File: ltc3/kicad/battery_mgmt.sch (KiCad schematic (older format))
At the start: 81 parts, among them Q1 Q_NMOS_DGS, Q2 Q_NMOS_DGS, Q3 Q_NMOS_DGS, Q4 Q_NMOS_DGS

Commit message: Deleted "Power Sources" sheet.
Moved what little circuity it contained into the "Battery Charging"
and "Battery Balancing" sheets.
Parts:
- added P?: LAB_IN, symbol CONN_01X02
- added R? (x2): R4T, symbol R4T
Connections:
- net labels added: BB_VSENSE_BATT+, BB_VSENSE_BATT-, BB_VSENSE_PV+, BB_VSENSE_PV-, VCC_BATT
- wire segments 204 -> 218
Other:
- note added: "R_sense = 1/Imax**2\n1 A = 1 ohm\n3 A = 0.1 ohm\n5 A = 0.04 ohms\n10 A = 0.01 ohms"
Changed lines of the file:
@@
 $Descr B 17000 11000
 encoding utf-8
-Sheet 8 9
-Title "Battery Charging"
+Sheet 8 8
+Title "Power In, Battery Management"
 Date "2015-10-24"
 Rev "A"
@@
 	1    0    0    -1
 $EndComp
-Text Notes 1400 9500 0    100  ~ 0
+Text Notes 2900 10250 0    100  ~ 0
 TODO:\n* Add feedback resistor disconnect circuit (datasheet fig. 27).
 Text Label 15350 8200 0    60   ~ 0
@@
 Text Label 5850 2550 2    60   ~ 0
 CSP
+$Comp
+L CONN_01X02 P?
+U 1 1 56357D56
+P 850 9850
+F 0 "P?" H 850 10000 50  0000 C CNN
+F 1 "LAB_IN" V 950 9850 50  0000 C CNN
+F 2 "" H 850 9850 60  0000 C CNN
+F 3 "" H 850 9850 60  0000 C CNN
+	1    850  9850
+	-1   0    0    1
+$EndComp
+Connection ~ 2050 9000
+Wire Wire Line
+	2050 9000 2050 9550
+Wire Wire Line
+	1950 9000 2300 9000
+Wire Wire Line
+	1300 9000 1650 9000
+Text HLabel 2300 9300 2    60   Output ~ 0
+BB_VSENSE_PV-
+Text HLabel 2300 9200 2    60   Output ~ 0
+BB_VSENSE_PV+
+$Comp
+L R4T R?
+U 1 1 5635AA23
+P 1800 9000
+F 0 "R?" V 1750 8850 50  0000 C CNN
+F 1 "R4T" V 1800 9000 50  0000 C CNN
+F 2 "" V 1730 9000 30  0000 C CNN
+F 3 "" H 1800 9000 30  0000 C CNN
+F 4 "1W 1%" V 1700 9100 60  0000 C CNN "Note"
+	1    1800 9000
+	0    1    1    0
+$EndComp
+Wire Wire Line
+	2300 9200 1750 9200
+Wire Wire Line
+	1750 9200 1750 9100
+Wire Wire Line
+	1850 9100 1850 9300
+Wire Wire Line
+	1850 9300 2300 9300
+Text HLabel 15400 700  2    60   Output ~ 0
+VCC_BATT
+Connection ~ 15150 700
+Wire Wire Line
+	15150 700  15150 1250
+Wire Wire Line
+	15050 700  15400 700
+Wire Wire Line
+	14400 700  14750 700
+Text HLabel 15400 1000 2    60   Output ~ 0
+BB_VSENSE_BATT-
+Text HLabel 15400 900  2    60   Output ~ 0
+BB_VSENSE_BATT+
+Text Notes 14750 2250 0    100  ~ 0
+R_sense = 1/Imax**2\n1 A = 1 ohm\n3 A = 0.1 ohm\n5 A = 0.04 ohms\n10 A = 0.01 ohms
+$Comp
+L R4T R?
+U 1 1 5635B0F2
+P 14900 700
+F 0 "R?" V 14850 550 50  0000 C CNN
+F 1 "R4T" V 14900 700 50  0000 C CNN
+F 2 "" V 14830 700 30  0000 C CNN
+F 3 "" H 14900 700 30  0000 C CNN
+F 4 "1W 1%" V 14800 800 60  0000 C CNN "Note"
+	1    14900 700
+	0    1    1    0
+$EndComp
+Wire Wire Line
+	15400 900  14850 900
+Wire Wire Line
+	14850 900  14850 800
+Wire Wire Line
+	15400 1000 14950 1000
+Wire Wire Line
+	14950 1000 14950 800
 $EndSCHEMATC

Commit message: More progress on cleaning up battery management circuit.
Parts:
- removed C?: 470n, symbol C
- removed Ccspout?, Cout?: C, symbol C
- removed R?: 10, symbol R
- removed Rsense?: 4.36m, symbol R
- added COUT4: 1μ, symbol C
- renumbered Cout1 to COUT1, Cout2a to COUT2A, Cout2b to COUT2B
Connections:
- net labels added: EXTVCC
- wire segments 218 -> 293
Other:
- moved on the sheet: C?, CCSPOUT, COUT1, COUT2A, COUT2B, R?, Rsense?

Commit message: Finished cleaning up battery management (LT8490) schematic.
High probability of errors, and certainly still room for improvement,
but I want to get the work on this branch merged back to the trunk.
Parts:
- removed Rsense?: 21m, symbol R
- removed Rsense?: 4.36m, symbol R
- added C?: 68n, symbol C
- added CIN4: 2.2µ, symbol C
- added R?: 53.6k, symbol R
- R?: value R4T -> 21m
- R?: value R4T -> 4.36m
- gave numbers to parts that had none: 1
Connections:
- net labels added: /SHDN, EXTV_CC, FAULT, FBIN, FBIW, RT, STATUS, VIN, VINR, VOUT
- net labels removed: Battery(+), PV+
- wire segments 293 -> 212
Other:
- note added: "FIXME: Safe to use one current-sense resistor\n for both the LT8490 and the LTC2991?"
- note added: "Place close to VIN."
- note removed: "R_sense = 1/Imax**2\n1 A = 1 ohm\n3 A = 0.1 ohm\n5 A = 0.04 ohms\n10 A = 0.01 ohms"
- moved on the sheet: C?, CCSPOUT, CIN1A, CIN1B, CIN1C, CIN2A, CIN2B, CIN2C, CIN3A, CIN3B, COUT1, COUT2A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

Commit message: More clean-up of battery-related sheets.
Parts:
- gave numbers to parts that had none: 6
- renumbered CIN1C to C?, CIN2C to C?, CIN3A to C?, COUT3B to C?, COUT2A to C?, COUT1 to C?, COUT2B to C?, CIN1B to C?, CIN1A to C?, CIN2B to C?, CIN2A to C?, CIN3B to C?, CCSPOUT to C?, COUT3A to C?, CIN4 to C?, COUT4 to C?, DB1 to D?, DB2 to D?
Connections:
- net BB_VSENSE_BATT+ renamed CSPOUT
- net BB_VSENSE_BATT- renamed CSNOUT
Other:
- note added: "CCSPOUT"
- note added: "CIN1"
- note added: "CIN2"
- note added: "CIN3"
- note added: "CIN4"
- note added: "COUT1"
- note added: "COUT2"
- note added: "COUT3"
- note added: "Place close\nto VIN."
- note removed: "Place close to VIN."
- moved on the sheet: C?, P?

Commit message: Re-ordered LTC3 schematic sheets; annotated battery management components.
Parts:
- gave numbers to parts that had none: 76
- renumbered L1 to L201, Q1 to Q201, Q4 to Q202, Q2 to Q203, Q3 to Q204

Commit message: LTC3: Updated batt mgmt feedback component values.
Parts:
- C223: renamed from C225; value .2532 µF -> .18µ
- C231: renamed from C226; value .3013µF -> .33µ
- R208: renamed from R224; Note (none) -> 1%
- R210: renamed from R228; value 8.06k -> 8k06; Note (none) -> 1%
- R214: renamed from R213; value 203.92k -> 294k
- R216: value 7.899k -> 11k5
- R217: value 39.49k -> 57k6
- R220: renamed from R219; value 7k -> 10k2
- R221: renamed from Rfbin201; value 94.725k -> 93k1
- R223: renamed from R214; value 7.731k -> 7k68
- R224: renamed from R215; value 16.592k -> 16k5
- R227: renamed from R218; value 3.318k -> 3k32
- renumbered C223 to C220, C224 to C221, C227 to C224, C228 to C225, C229 to C226, C230 to C227, C231 to C228, C220 to C229, C221 to C230, D203 to D201, D204 to D202, D201 to D203, D202 to D204, R208 to R209, R209 to R213, R225 to R215, R210 to R218, R229 to R219, R220 to R222, R222 to R225, R223 to R226, R226 to R228, R227 to R229, R221 to R233, R233 to R234
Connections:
- net GND: now also R223.2; no longer C231.2
- net /SHDN: no longer names the net of R215.2, R219.1, U201.11 (SHDN)
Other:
- note added: "202kHz switch"
- note added: "CDACI"
- note added: "RDAC01"
- note added: "RDAC02"
- note added: "RDACI1"
- note added: "RDACI2"
- note added: "RFBIN1"
- note added: "RFBIN2"
- note added: "RFBOUT1"
- note added: "RFBOUT2"
- note added: "TODO:\n* Add DC supply detection circuit (datasheet p. 35).\n* Add feedback resistor disconnect circuit (datasheet fig. 27)."
- note removed: "TODO:\n* Add feedback resistor disconnect circuit (datasheet fig. 27)."
- moved on the sheet: C201, C202, C203, C204, C205, C206, C207, C208, C209, C210, C211, C212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

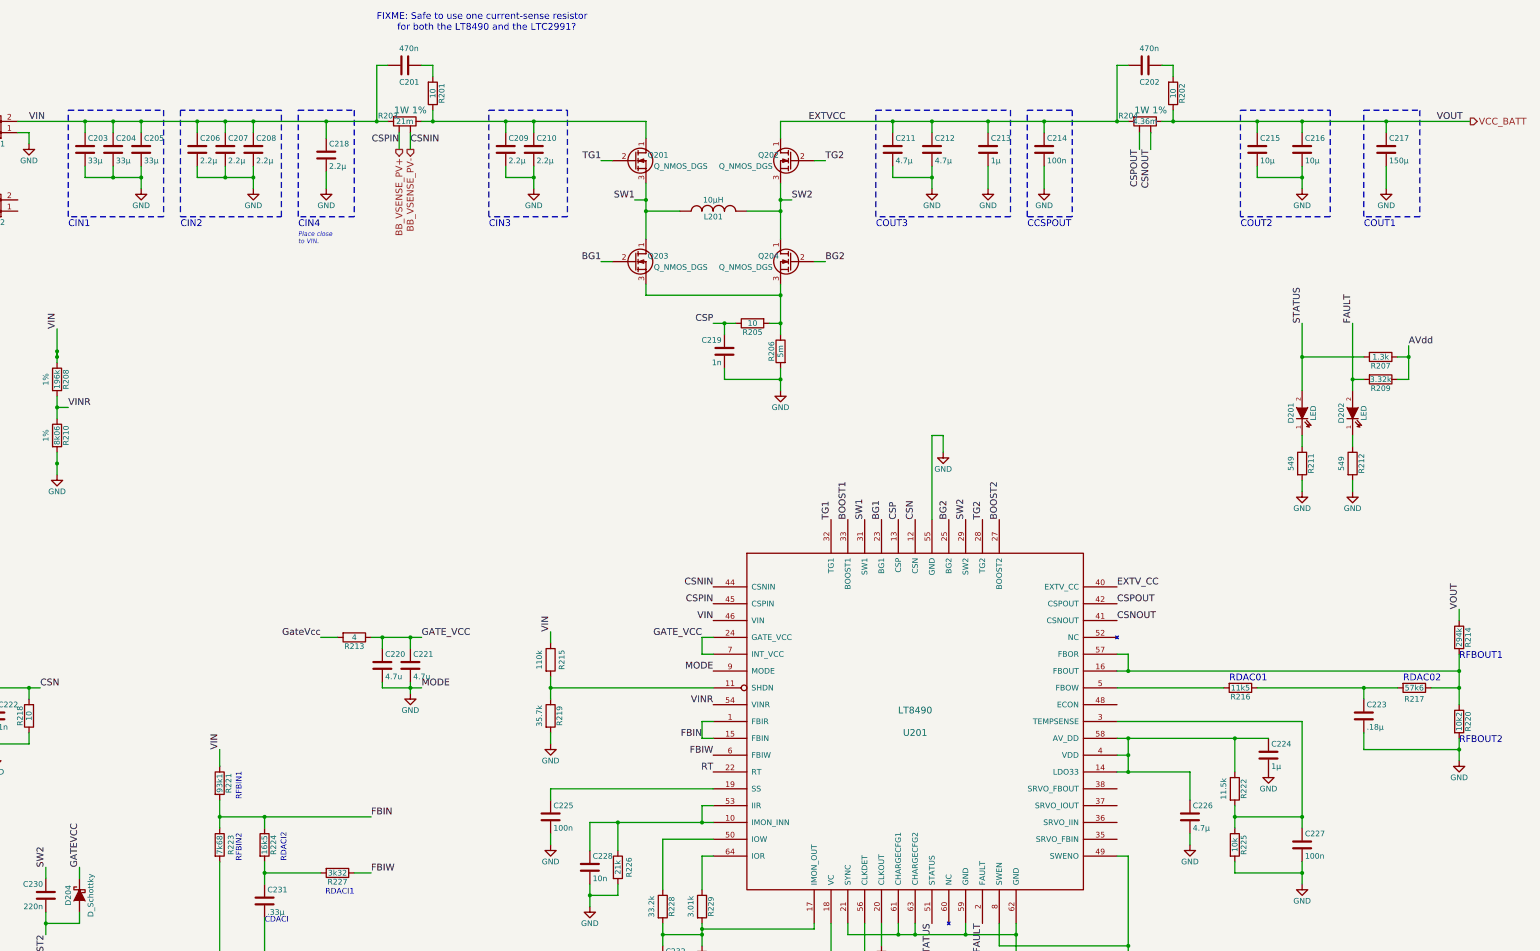
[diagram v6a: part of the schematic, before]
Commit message: LTC3: First take at adding datasheet references to batt mgmt schematic.
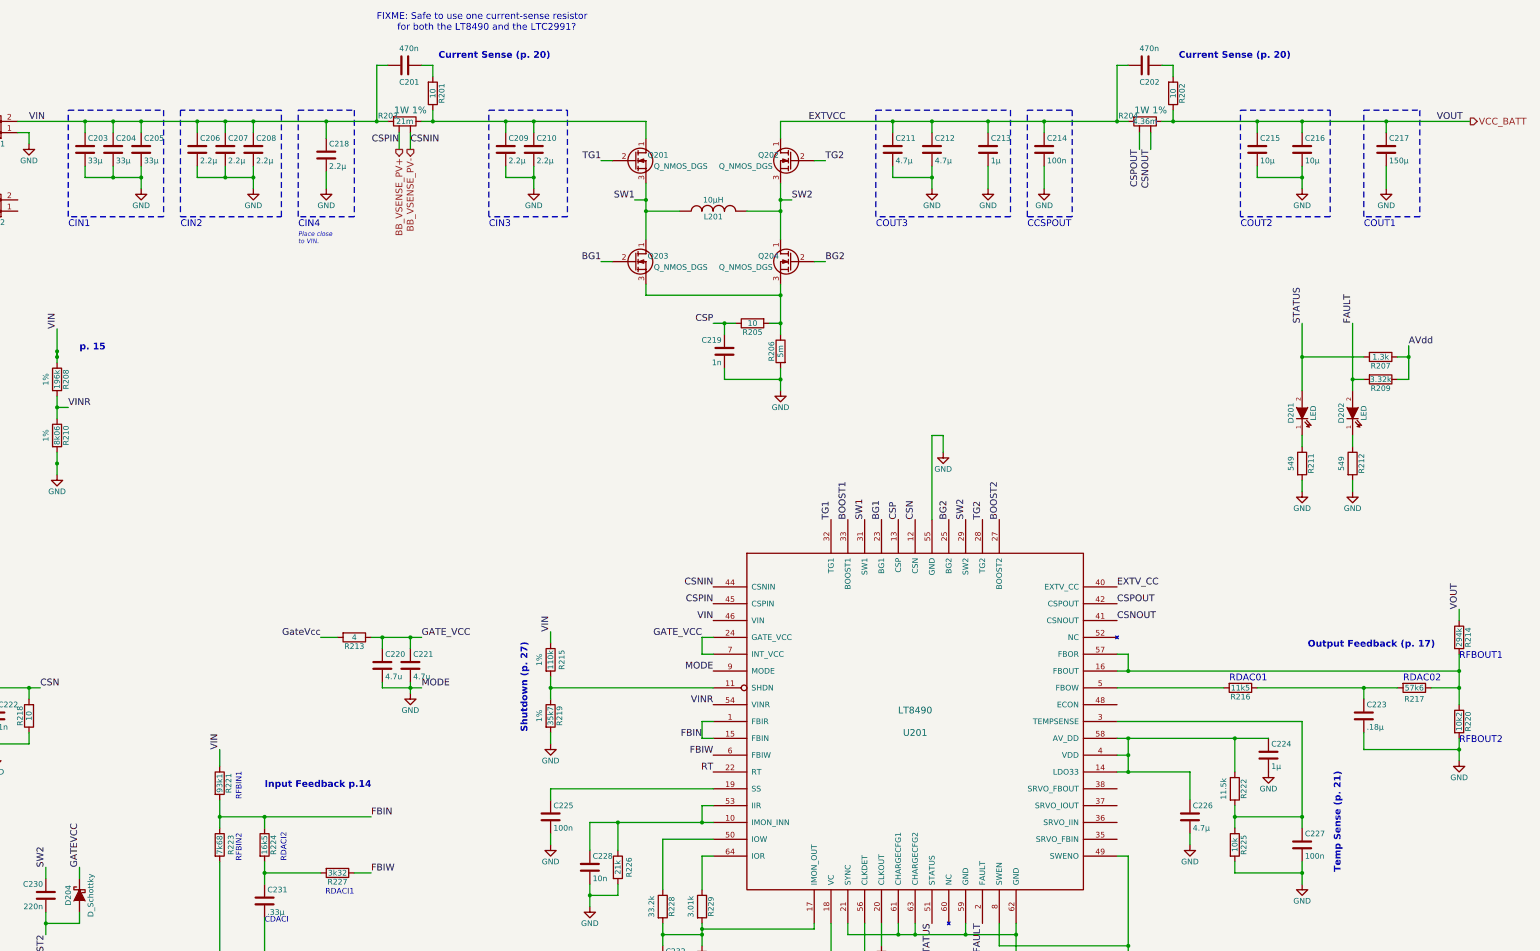
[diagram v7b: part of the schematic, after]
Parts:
- R215: Note (none) -> 1%
- R219: value 35.7k -> 35k7; Note (none) -> 1%
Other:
- note added: "Current Sense (p. 20)"
- note added: "Input Feedback p.14"
- note added: "Output Feedback (p. 17)"
- note added: "Shutdown (p. 27)"
- note added: "Temp Sense (p. 21)"
- note added: "p. 15"
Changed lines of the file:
@@
 P 6750 6650
 F 0 "R215" V 6850 6650 50  0000 C CNN
-F 1 "110k" V 6650 6650 50  0000 C CNN
+F 1 "110k" V 6750 6650 50  0000 C CNN
 F 2 "" V 6680 6650 30  0000 C CNN
 F 3 "" H 6750 6650 30  0000 C CNN
+F 4 "1%" V 6650 6650 50  0000 C CNN "Note"
 	1    6750 6650
 	1    0    0    -1
@@
 P 6750 7150
 F 0 "R219" V 6830 7150 50  0000 C CNN
-F 1 "35.7k" V 6650 7150 50  0000 C CNN
+F 1 "35k7" V 6750 7150 50  0000 C CNN
 F 2 "" V 6680 7150 30  0000 C CNN
 F 3 "" H 6750 7150 30  0000 C CNN
+F 4 "1%" V 6650 7150 50  0000 C CNN "Note"
 	1    6750 7150
 	1    0    0    -1
@@
 Text Notes 4550 9650 0    60   Italic 0
 202kHz switch
+Text Notes 4200 7800 0    60   ~ 12
+Input Feedback p.14
+Text Notes 2550 3900 0    60   ~ 12
+p. 15
+Text Notes 13500 6550 0    60   ~ 12
+Output Feedback (p. 17)
+Text Notes 5750 1300 0    60   ~ 12
+Current Sense (p. 20)
+Text Notes 12350 1300 0    60   ~ 12
+Current Sense (p. 20)
+Text Notes 6550 7300 1    60   ~ 12
+Shutdown (p. 27)
+Text Notes 13800 8550 1    60   ~ 12
+Temp Sense (p. 21)
 $EndSCHEMATC

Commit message: LTC3: Added lab power input to batt mgmt schematic.
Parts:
- added D201, D202: D_Schottky, symbol D_Schottky
- added Q203: Q_NPN_BCE, symbol Q_NPN_BCE
- added R206: 100k, symbol R
- added R208: 33k, symbol R
- renumbered D201 to D203, D202 to D204, D203 to D205, D204 to D206, Q203 to Q204, Q204 to Q205, R208 to R205, R210 to R207, R205 to R209, R206 to R210, R207 to R211, R209 to R212, R211 to R218, R212 to R219, R218 to R220, R219 to R221, R220 to R222, R221 to R223, R222 to R224, R223 to R225, R224 to R226, R225 to R227, R226 to R228, R227 to R229, R228 to R230, R229 to R231, R230 to R232, R231 to R233, R232 to R234, R233 to R235, R234 to R236
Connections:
- net GND: now also P202.1 (P1), Q203.3 (E), R208.2
- net VIN: now also D201.1 (K); no longer P201.2 (P2)
- net VINR: now also Q203.2 (C)
- net at P202.2 (P2): now also D202.2 (A)
- new net: D201.2 (A), P201.2 (P2)
- new net: D202.1 (K), R206.1
- new net: Q203.1 (B), R206.2, R208.1
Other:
- note added: "p. 15, p. 34"
- note removed: "p. 15"
- moved on the sheet: C201, C202, C203, C204, C205, C206, C207, C208, C209, C210, C211, C212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
